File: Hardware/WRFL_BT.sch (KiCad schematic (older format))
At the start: 5 parts, among them U8 HM-10

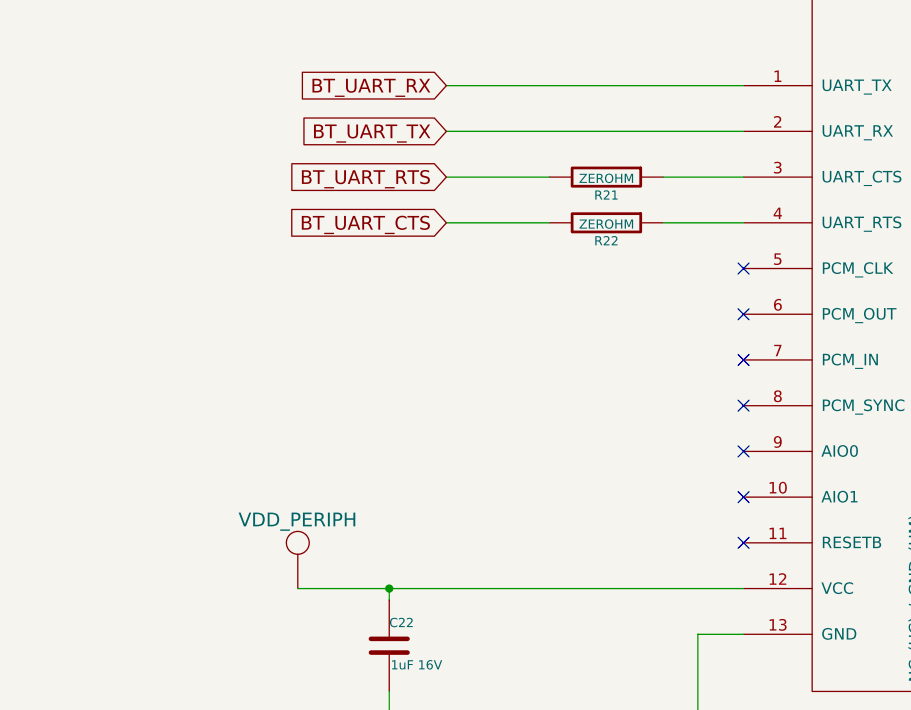
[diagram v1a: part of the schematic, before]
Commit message: MCU function assignment
BT RTS/CTS as test points,
BT reset GPIO option
Launchpad header pin function assignment (for ERC check)
Power symbols corrections
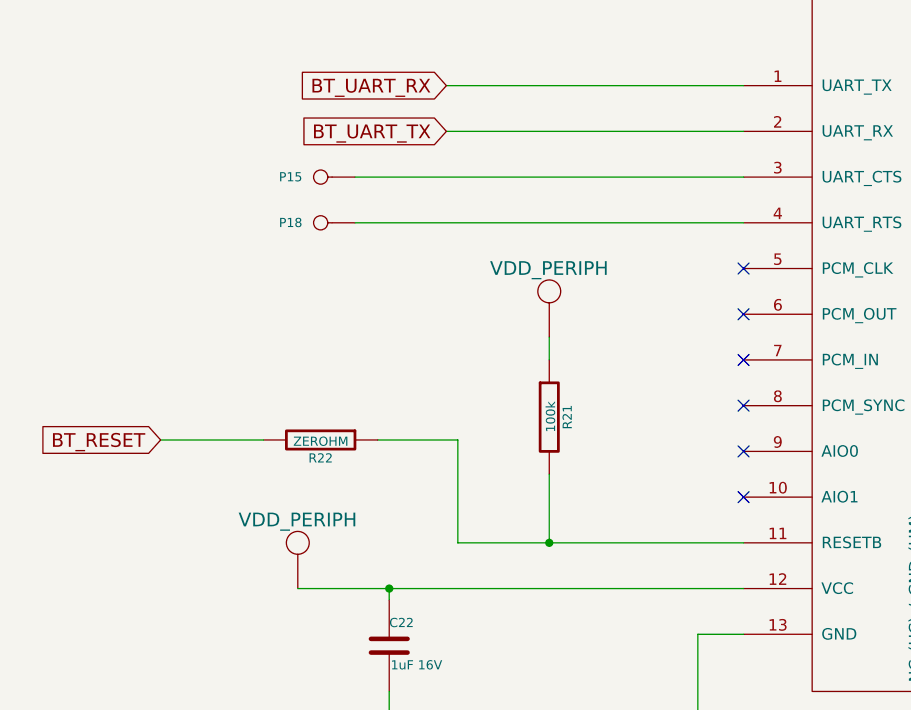
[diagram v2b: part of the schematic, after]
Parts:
- added P15, P18: TEST_POINT, symbol CONN_1
- R21: value ZEROHM -> 100k
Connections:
- net BT_UART_RTS is gone; now on an unnamed net: R21.2
- net VDD_PERIPH: now also R21.1
- net at U8.11 (RESETB): now also R22.1
- net at U8.3 (UART_CTS): now also P15.1; no longer R21.1
- net at U8.4 (UART_RTS): now also P18.1; no longer R22.1
- net BT_UART_CTS renamed BT_RESET
- no-connect marks 24 -> 23
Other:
- moved on the sheet: R22
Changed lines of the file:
@@
-EESchema Schematic File Version 2  date Tuesday, October 15, 2013 09:37:22 AM
+EESchema Schematic File Version 2  date Tuesday, October 22, 2013 02:02:38 PM
 LIBS:power
 LIBS:device
@@
 Sheet 6 6
 Title ""
-Date "15 oct 2013"
+Date "22 oct 2013"
 Rev ""
 Comp "Nightmechanic"
@@
 $EndComp
 $Comp
-L VDD_PERIPH #U23
+L VDD_PERIPH #U081
 U 1 1 52571F8F
 P 2100 4600
-F 0 "#U23" H 2100 4800 60  0001 C CNN
+F 0 "#U081" H 2100 4800 60  0001 C CNN
 F 1 "VDD_PERIPH" H 2100 4700 60  0000 C CNN
 F 2 "~" H 2100 4600 60  0000 C CNN
@@
 $EndComp
 $Comp
-L GND #PWR52
+L GND #PWR082
 U 1 1 52571FBC
 P 3850 5350
-F 0 "#PWR52" H 3850 5350 30  0001 C CNN
+F 0 "#PWR082" H 3850 5350 30  0001 C CNN
 F 1 "GND" H 3850 5280 30  0001 C CNN
 F 2 "" H 3850 5350 60  0000 C CNN
@@
 $EndComp
 $Comp
-L GND #PWR53
+L GND #PWR083
 U 1 1 52571FCB
 P 4800 5850
-F 0 "#PWR53" H 4800 5850 30  0001 C CNN
+F 0 "#PWR083" H 4800 5850 30  0001 C CNN
 F 1 "GND" H 4800 5780 30  0001 C CNN
 F 2 "" H 4800 5850 60  0000 C CNN
@@
 $EndComp
 $Comp
-L GND #PWR54
+L GND #PWR084
 U 1 1 52571FDA
 P 6200 5800
-F 0 "#PWR54" H 6200 5800 30  0001 C CNN
+F 0 "#PWR084" H 6200 5800 30  0001 C CNN
 F 1 "GND" H 6200 5730 30  0001 C CNN
 F 2 "" H 6200 5800 60  0000 C CNN
@@
 $EndComp
 $Comp
-L GND #PWR55
+L GND #PWR085
 U 1 1 52571FE9
 P 7200 5250
-F 0 "#PWR55" H 7200 5250 30  0001 C CNN
+F 0 "#PWR085" H 7200 5250 30  0001 C CNN
 F 1 "GND" H 7200 5180 30  0001 C CNN
 F 2 "" H 7200 5250 60  0000 C CNN
@@
 $EndComp
 $Comp
-L VDD_PERIPH #U24
+L VDD_PERIPH #U086
 U 1 1 52571FF6
 P 8700 4500
-F 0 "#U24" H 8700 4700 60  0001 C CNN
+F 0 "#U086" H 8700 4700 60  0001 C CNN
 F 1 "VDD_PERIPH" H 8700 4600 60  0000 C CNN
 F 2 "~" H 8700 4500 60  0000 C CNN
@@
 Connection ~ 2500 4800
 $Comp
-L GND #PWR51
+L GND #PWR087
 U 1 1 5257201B
 P 2500 5350
-F 0 "#PWR51" H 2500 5350 30  0001 C CNN
+F 0 "#PWR087" H 2500 5350 30  0001 C CNN
 F 1 "GND" H 2500 5280 30  0001 C CNN
 F 2 "" H 2500 5350 60  0000 C CNN
@@
 NoConn ~ 4050 4200
 NoConn ~ 4050 4400
-NoConn ~ 4050 4600
 Text GLabel 2750 2600 0    60   Input ~ 0
 BT_UART_RX
 Text GLabel 2750 2800 0    60   Input ~ 0
 BT_UART_TX
-Text GLabel 2750 3000 0    60   Input ~ 0
-BT_UART_RTS
-Text GLabel 2750 3200 0    60   Input ~ 0
-BT_UART_CTS
+Text GLabel 1500 4150 0    60   Input ~ 0
+BT_RESET
 $Comp
 L R R22
 U 1 1 5257207A
-P 3450 3200
-F 0 "R22" V 3530 3200 40  0000 C CNN
-F 1 "ZEROHM" V 3457 3201 40  0000 C CNN
-F 2 "0805" V 3380 3200 30  0001 C CNN
-F 3 "~" H 3450 3200 30  0000 C CNN
-	1    3450 3200
+P 2200 4150
+F 0 "R22" V 2280 4150 40  0000 C CNN
+F 1 "ZEROHM" V 2207 4151 40  0000 C CNN
+F 2 "0805" V 2130 4150 30  0001 C CNN
+F 3 "~" H 2200 4150 30  0000 C CNN
+	1    2200 4150
 	0    1    1    0
 $EndComp
+Wire Wire Line
+	2750 2600 4050 2600
+Wire Wire Line
+	4050 2800 2750 2800
+Wire Wire Line
+	2350 3000 4050 3000
+Wire Wire Line
+	1950 4150 1500 4150
 $Comp
 L R R21
-U 1 1 5257208C
-P 3450 3000
-F 0 "R21" V 3530 3000 40  0000 C CNN
-F 1 "ZEROHM" V 3457 3001 40  0000 C CNN
-F 2 "0805" V 3380 3000 30  0001 C CNN
-F 3 "~" H 3450 3000 30  0000 C CNN
-	1    3450 3000
-	0    1    1    0
-$EndComp
-Wire Wire Line
-	2750 2600 4050 2600
-Wire Wire Line
-	4050 2800 2750 2800
-Wire Wire Line
-	2750 3000 3200 3000
-Wire Wire Line
-	3700 3000 4050 3000
-Wire Wire Line
-	4050 3200 3700 3200
-Wire Wire Line
-	3200 3200 2750 3200
+U 1 1 526452CC
+P 3200 4050
+F 0 "R21" V 3280 4050 40  0000 C CNN
+F 1 "100k" V 3207 4051 40  0000 C CNN
+F 2 "0805" V 3130 4050 30  0001 C CNN
+F 3 "~" H 3200 4050 30  0000 C CNN
+	1    3200 4050
+	1    0    0    -1
+$EndComp
+$Comp
+L VDD_PERIPH #U088
+U 1 1 526452D2
+P 3200 3500
+F 0 "#U088" H 3200 3700 60  0001 C CNN
+F 1 "VDD_PERIPH" H 3200 3600 60  0000 C CNN
+F 2 "~" H 3200 3500 60  0000 C CNN
+F 3 "~" H 3200 3500 60  0000 C CNN
+	1    3200 3500
+	1    0    0    -1
+$EndComp
+Wire Wire Line
+	2800 4600 4050 4600
+Wire Wire Line
+	3200 4600 3200 4300
+Wire Wire Line
+	3200 3700 3200 3800
+Wire Wire Line
+	2450 4150 2800 4150
+Wire Wire Line
+	2800 4150 2800 4600
+Connection ~ 3200 4600
+$Comp
+L CONN_1 P15
+U 1 1 5264532F
+P 2200 3000
+F 0 "P15" H 2280 3000 40  0000 L CNN
+F 1 "TEST_POINT" H 2200 3055 30  0001 C CNN
+F 2 "" H 2200 3000 60  0000 C CNN
+F 3 "" H 2200 3000 60  0000 C CNN
+	1    2200 3000
+	-1   0    0    1
+$EndComp
+$Comp
+L CONN_1 P18
+U 1 1 52645349
+P 2200 3200
+F 0 "P18" H 2280 3200 40  0000 L CNN
+F 1 "TEST_POINT" H 2200 3255 30  0001 C CNN
+F 2 "" H 2200 3200 60  0000 C CNN
+F 3 "" H 2200 3200 60  0000 C CNN
+	1    2200 3200
+	-1   0    0    1
+$EndComp
+Wire Wire Line
+	2350 3200 4050 3200
 $EndSCHEMATC
